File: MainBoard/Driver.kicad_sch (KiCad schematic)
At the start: 4 parts, among them U3 IS31FL3729-QFLS4-TR

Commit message: Move main PCB into subdirectory so that we can add a bezel PCB to this repo
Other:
- company: Framework Computer Inc -> C. Scott Ananian
- title: LED Matrix Input Module - LED Driver -> Seven Segment Display Input Module
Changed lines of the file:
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@@
 	(paper "A4")
 	(title_block
-		(title "LED Matrix Input Module - LED Driver")
-		(date "2022-12-18")
-		(company "Framework Computer Inc")
+		(title "Seven Segment Display Input Module")
+		(date "2024-07-13")
+		(company "C. Scott Ananian")
 		(comment 1 "This work is licensed under a Creative Commons Attribution 4.0 International License")
-		(comment 2 "https://github.com/FrameworkComputer/InputModules")
-		(comment 3 "https://frame.work")
+		(comment 2 "https://github.com/cscott/SevenSegmentInputModule")
+		(comment 3 "https://cscott.net")
 	)
 	(junction
@@
 		)
 		(instances
-			(project "SevenSegment"
+			(project "MainBoard"
 				(path "/2fa7b4ce-e682-4c2e-9419-b1318fe8c56d/811b33f2-c0b3-41a3-829f-026bb0f90e22"
 					(page "3")

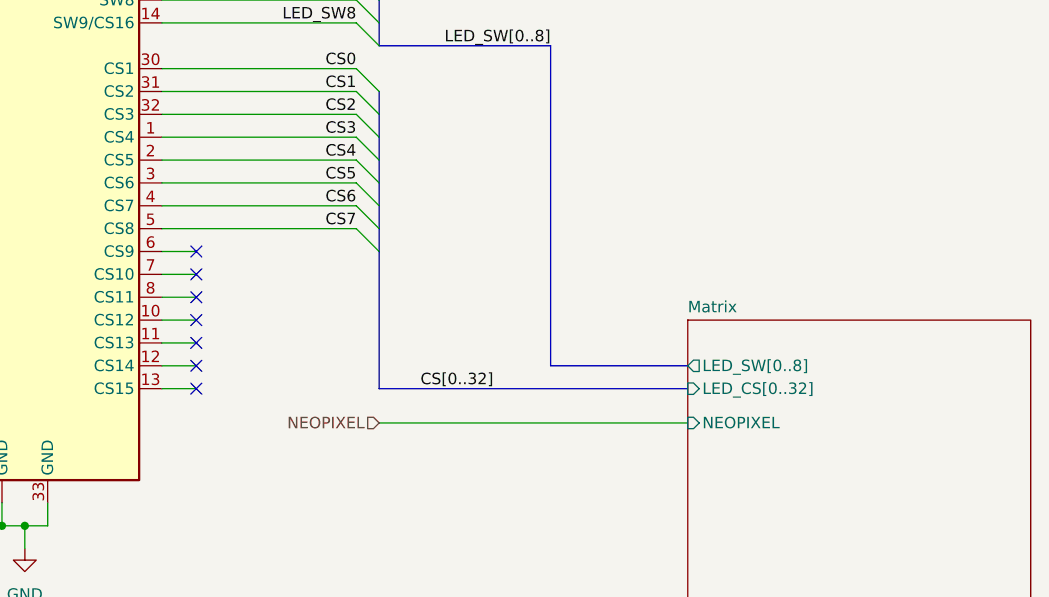
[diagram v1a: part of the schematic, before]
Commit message: Use 'dumb' 3.1V white LEDs instead of neopixels for legend backlighting
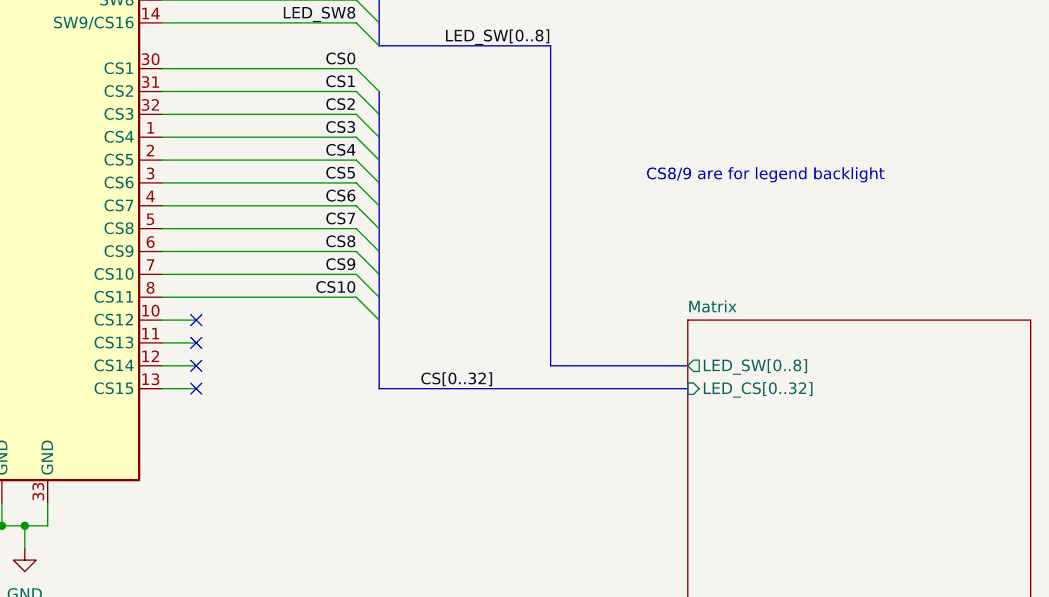
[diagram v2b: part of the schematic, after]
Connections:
- net CS8: now reaches U3.6 (CS9)
- net CS9: now reaches U3.7 (CS10)
- net CS10: now reaches U3.8 (CS11)
- no-connect marks 7 -> 4
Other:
- sheet Matrix ports: added none; removed NEOPIXEL
- note added: "CS8/9 are for legend backlight"
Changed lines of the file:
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@@
-	)
-	(no_connect
-		(at 105.41 97.79)
 	)
 	(no_connect
@@
 	)
 	(no_connect
-		(at 105.41 100.33)
-	)
-	(no_connect
-		(at 105.41 95.25)
-	)
-	(no_connect
 		(at 105.41 110.49)
 	)
@@
 	)
 	(bus_entry
+		(at 123.19 100.33)
+		(size 2.54 2.54)
+		(stroke
+			(width 0)
+			(type default)
+		)
+	)
+	(bus_entry
 		(at 123.19 62.23)
 		(size 2.54 2.54)
@@
 	)
 	(bus_entry
+		(at 123.19 95.25)
+		(size 2.54 2.54)
+		(stroke
+			(width 0)
+			(type default)
+		)
+	)
+	(bus_entry
 		(at 123.19 92.71)
 		(size 2.54 2.54)
@@
 	)
 	(bus_entry
+		(at 123.19 97.79)
+		(size 2.54 2.54)
+		(stroke
+			(width 0)
+			(type default)
+		)
+	)
+	(bus_entry
 		(at 123.19 74.93)
 		(size 2.54 2.54)
@@
 		)
 	)
-	(wire
-		(pts
-			(xy 101.6 95.25) (xy 105.41 95.25)
-		)
-		(stroke
-			(width 0)
-			(type default)
-		)
-	)
 	(bus
 		(pts
@@
 	(wire
 		(pts
+			(xy 101.6 97.79) (xy 123.19 97.79)
+		)
+		(stroke
+			(width 0)
+			(type default)
+		)
+	)
+	(wire
+		(pts
 			(xy 59.69 52.07) (xy 71.12 52.07)
 		)
@@
 		)
 	)
+	(bus
+		(pts
+			(xy 125.73 100.33) (xy 125.73 97.79)
+		)
+		(stroke
+			(width 0)
+			(type default)
+		)
+	)
 	(wire
 		(pts
@@
 		)
 	)
-	(wire
-		(pts
-			(xy 125.73 114.3) (xy 160.02 114.3)
-		)
-		(stroke
-			(width 0)
-			(type default)
-		)
-	)
 	(bus
 		(pts
@@
 		)
 	)
-	(wire
-		(pts
-			(xy 101.6 100.33) (xy 105.41 100.33)
-		)
-		(stroke
-			(width 0)
-			(type default)
-		)
-	)
-	(bus
-		(pts
-			(xy 125.73 110.49) (xy 125.73 95.25)
+	(bus
+		(pts
+			(xy 125.73 110.49) (xy 125.73 102.87)
 		)
 		(stroke
@@
 		)
 	)
+	(bus
+		(pts
+			(xy 125.73 102.87) (xy 125.73 100.33)
+		)
+		(stroke
+			(width 0)
+			(type default)
+		)
+	)
 	(wire
 		(pts
@@
 		)
 	)
+	(bus
+		(pts
+			(xy 125.73 97.79) (xy 125.73 95.25)
+		)
+		(stroke
+			(width 0)
+			(type default)
+		)
+	)
 	(wire
 		(pts
@@
 	(wire
 		(pts
-			(xy 101.6 97.79) (xy 105.41 97.79)
-		)
-		(stroke
-			(width 0)
-			(type default)
-		)
-	)
-	(wire
-		(pts
 			(xy 101.6 77.47) (xy 123.19 77.47)
 		)
@@
 		)
 	)
+	(wire
+		(pts
+			(xy 101.6 95.25) (xy 123.19 95.25)
+		)
+		(stroke
+			(width 0)
+			(type default)
+		)
+	)
 	(bus
 		(pts
@@
 	(wire
 		(pts
+			(xy 101.6 100.33) (xy 123.19 100.33)
+		)
+		(stroke
+			(width 0)
+			(type default)
+		)
+	)
+	(wire
+		(pts
 			(xy 71.12 33.02) (xy 62.23 33.02)
 		)
@@
 			(width 0)
 			(type default)
+		)
+	)
+	(text "CS8/9 are for legend backlight"
+		(exclude_from_sim no)
+		(at 168.656 86.868 0)
+		(effects
+			(font
+				(size 1.27 1.27)
+			)
 		)
 	)
@@
 		)
 	)
+	(label "CS8"
+		(at 123.19 95.25 180)
+		(fields_autoplaced yes)
+		(effects
+			(font
+				(size 1.27 1.27)
+			)
+			(justify right bottom)
+		)
+	)
 	(label "LED_SW7"
 		(at 123.19 67.31 180)
@@
 		)
 	)
+	(label "CS10"
+		(at 123.19 100.33 180)
+		(fields_autoplaced yes)
+		(effects
+			(font
+				(size 1.27 1.27)
+			)
+			(justify right bottom)
+		)
+	)
 	(label "LED_SW3"
 		(at 123.19 57.15 180)
@@
 	(label "CS4"
 		(at 123.19 85.09 180)
+		(fields_autoplaced yes)
+		(effects
+			(font
+				(size 1.27 1.27)
+			)
+			(justify right bottom)
+		)
+	)
+	(label "CS9"
+		(at 123.19 97.79 180)
 		(fields_autoplaced yes)
 		(effects
@@
 		(shape input)
 		(at 59.69 57.15 180)
-		(fields_autoplaced yes)
-		(effects
-			(font
-				(size 1.27 1.27)
-			)
-			(justify right)
-		)
-	)
-	(hierarchical_label "NEOPIXEL"
-		(shape input)
-		(at 125.73 114.3 180)
 		(fields_autoplaced yes)
 		(effects
@@
 			(effects
 				(font
-					(size 1.27 1.27)
-				)
-				(justify left)
-			)
-		)
-		(pin "NEOPIXEL" input
-			(at 160.02 114.3 180)
-			(effects
-				(font
